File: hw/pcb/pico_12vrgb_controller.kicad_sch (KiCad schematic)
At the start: 20 parts, among them J1 Conn_01x04_RGB, J2 Conn_01x04_RGB, J3 Conn_01x04_RGB, J4 Conn_01x04_RGB, J5 Conn_01x03_Male, J6 Conn_01x03_Male, J7 Conn_01x15_SATA_PWR, Q1 DMG2302U, Q10 DMG2302U, Q11 DMG2302U, Q12 DMG2302U, Q2 DMG2302U, Q3 DMG2302U, Q4 DMG2302U, Q5 DMG2302U, Q6 DMG2302U, Q7 DMG2302U, Q8 DMG2302U, Q9 DMG2302U, U1 Raspberry_Pi_Pico

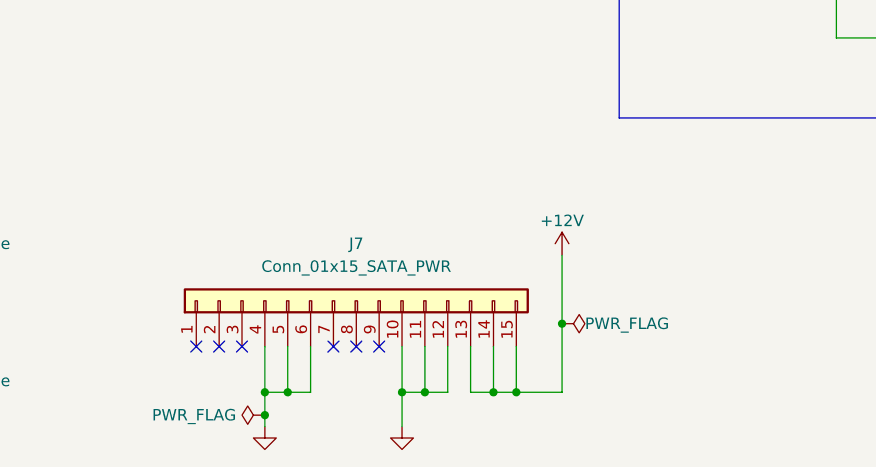
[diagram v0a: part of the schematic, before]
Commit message: Add custom model and footprint for SATA connector
I might need to change this, because the ModDIY listing shows two
different connectors in the pictures, but only has one data sheet
picture. Hopefully both connectors work with the same footprint.
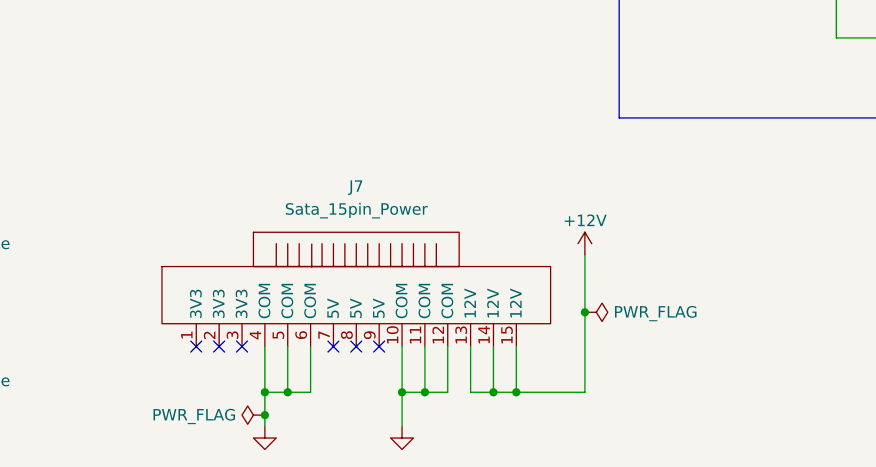
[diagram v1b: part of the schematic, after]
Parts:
- removed J7: Conn_01x15_SATA_PWR, symbol Connector_Generic:Conn_01x15
- added J7: Sata_15pin_Power, pico_12vrgb_controller:ModDIY_SATA_15pin_RightAngle_Header, symbol pico_12vrgb:Sata_15pin_Power
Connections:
- net +12V: now also J7.13 (12V), J7.14 (12V), J7.15 (12V)
- net GND: now also J7.10 (COM), J7.11 (COM), J7.12 (COM), J7.4 (COM), J7.5 (COM), J7.6 (COM)

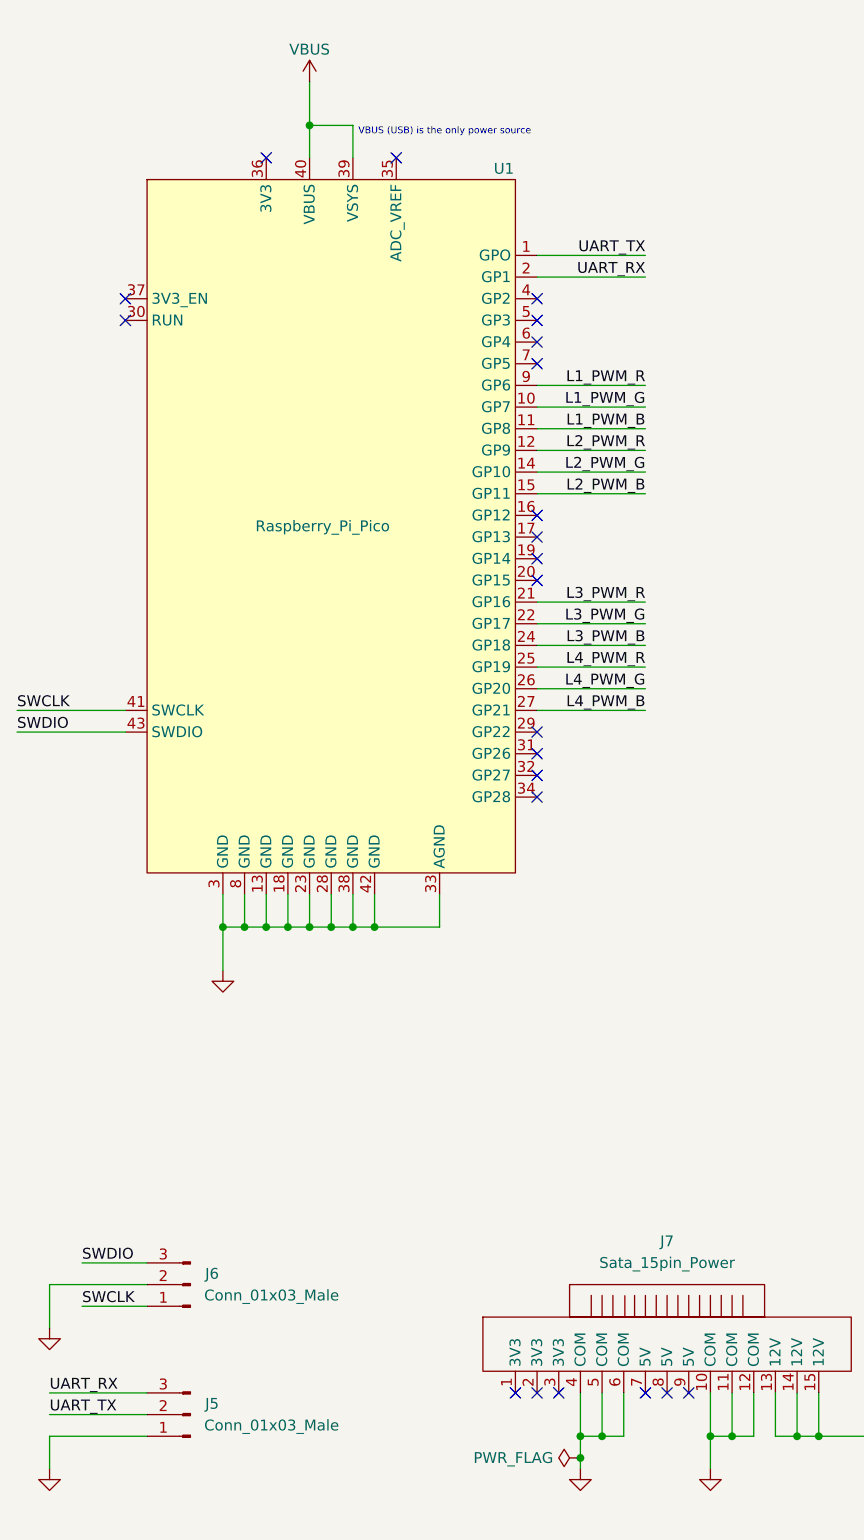
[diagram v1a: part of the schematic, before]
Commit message: Add ADC reference to schematic
Planning to use the internal temperature sensor and given the small
voltages involved, adding a reference sounds like a good idea.

Also changes the UART header to be 4 pins, which seems more conventional
even though the power pin will be disconnected.
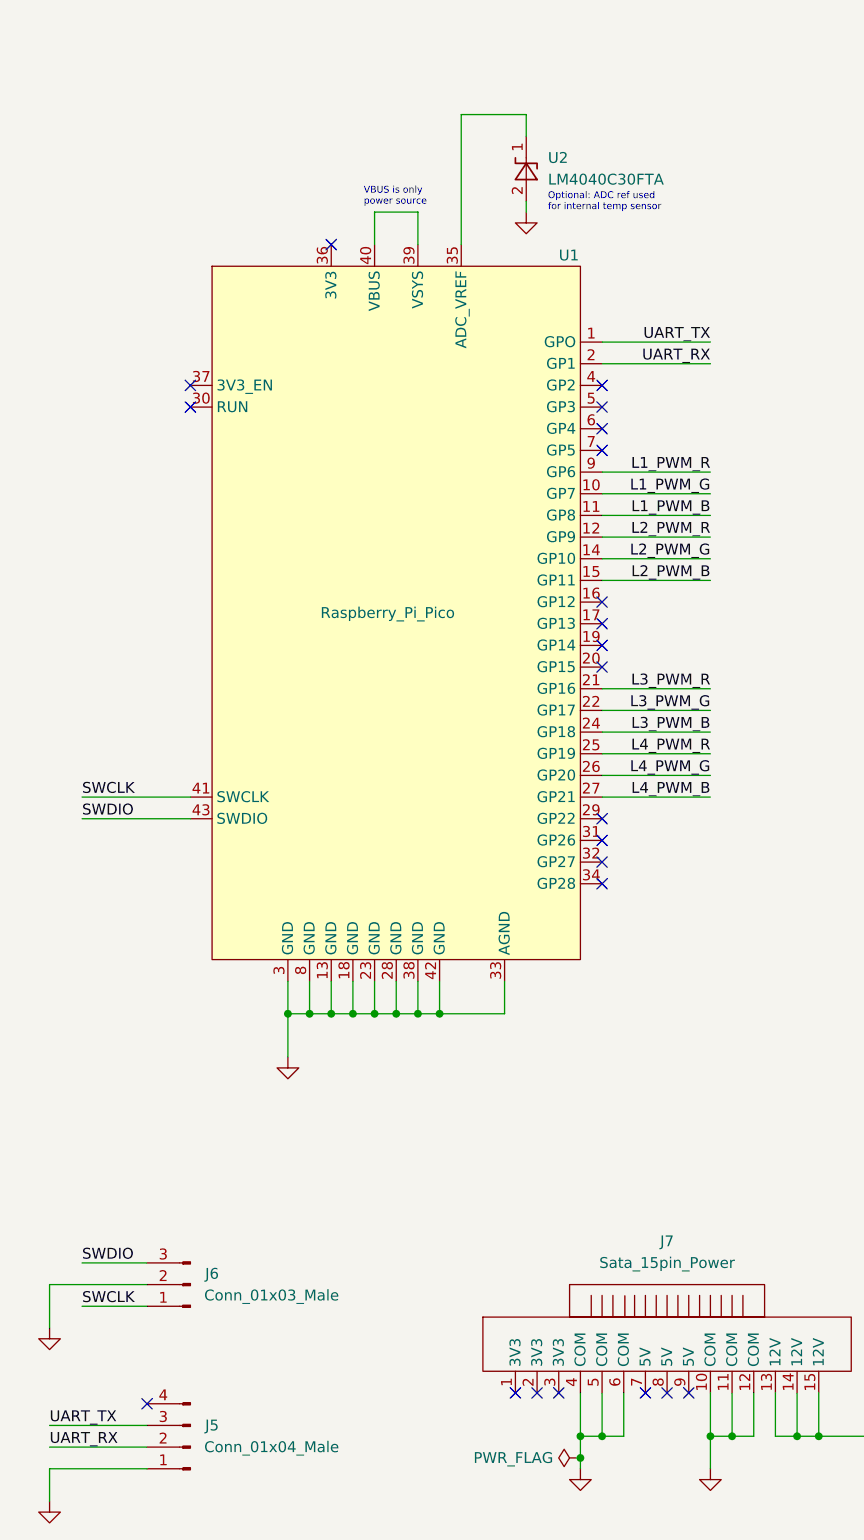
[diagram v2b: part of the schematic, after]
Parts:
- removed J5: Conn_01x03_Male, Connector_PinHeader_2.54mm:PinHeader_1x03_P2.54mm_Vertical, symbol Connector:Conn_01x03_Male
- added J5: Conn_01x04_Male, Connector_PinHeader_2.54mm:PinHeader_1x04_P2.54mm_Vertical, symbol Connector:Conn_01x04_Male
- added U2: LM4040C30FTA, Package_TO_SOT_SMD:SOT-23, symbol Reference_Voltage:LM4040DBZ-3
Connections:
- net GND: now also J5.1 (Pin_1), U2.2 (A)
- net UART_RX: now also J5.2 (Pin_2)
- net UART_TX: now also J5.3 (Pin_3)
- net at U1.35 (ADC_VREF): now also U2.1 (K)
- net VBUS: no longer names the net of U1.39 (VSYS), U1.40 (VBUS)
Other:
- note added: "Optional: ADC ref used for internal temp sensor"
- note added: "VBUS is only power source"
- note removed: "VBUS (USB) is the only power source"
- moved on the sheet: U1

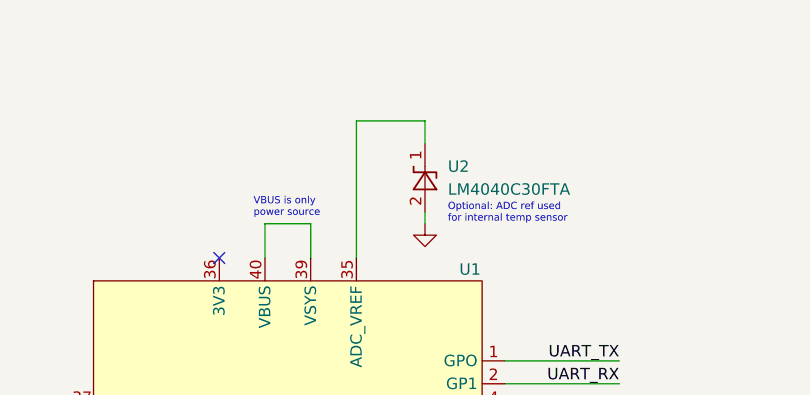
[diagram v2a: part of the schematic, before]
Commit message: Start routing PCB, change header orientation
The RGB half is mostly complete, although I might shift things around to
save a bit of space. Still need to connect things up to the Pico.
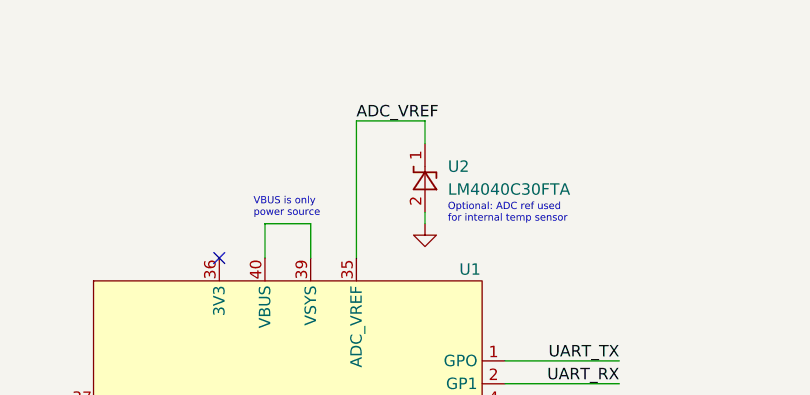
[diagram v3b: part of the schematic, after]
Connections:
- net ADC_VREF: now reaches U1.35 (ADC_VREF), U2.1 (K)
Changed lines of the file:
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@@
+    (effects (font (size 1.27 1.27)) (justify left bottom))
+  )
+  (label "ADC_VREF" (at 73.66 29.21 0)
     (effects (font (size 1.27 1.27)) (justify left bottom))
   )

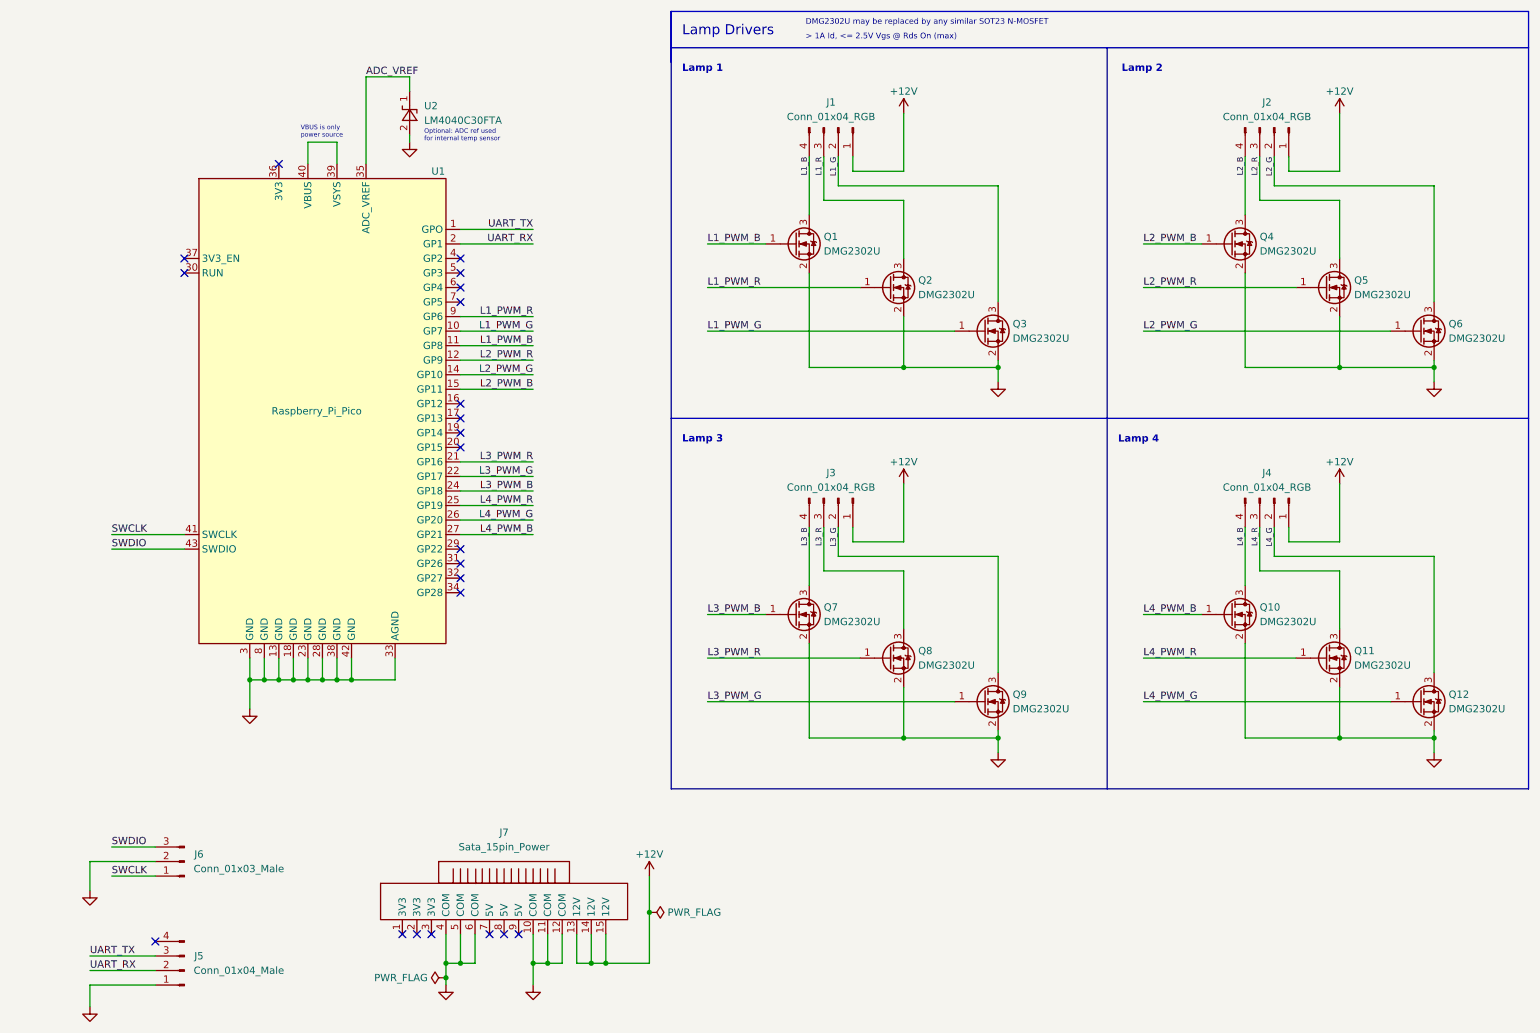
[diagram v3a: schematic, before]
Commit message: Finish PCB routing
Reduce the size of the PCB to 5 square inches, although I could probably
get it a bit smaller. Update the RGB header footprints with the correct
pin sizes and nice labels. Finally, reassign PWM pins to enable cleaner
routing.

There's a bunch of DRC failures because I drew a shape over some traces
instead of using a fill zone. I'll have to try this again and see if I
can get the fill zone to do what I want.
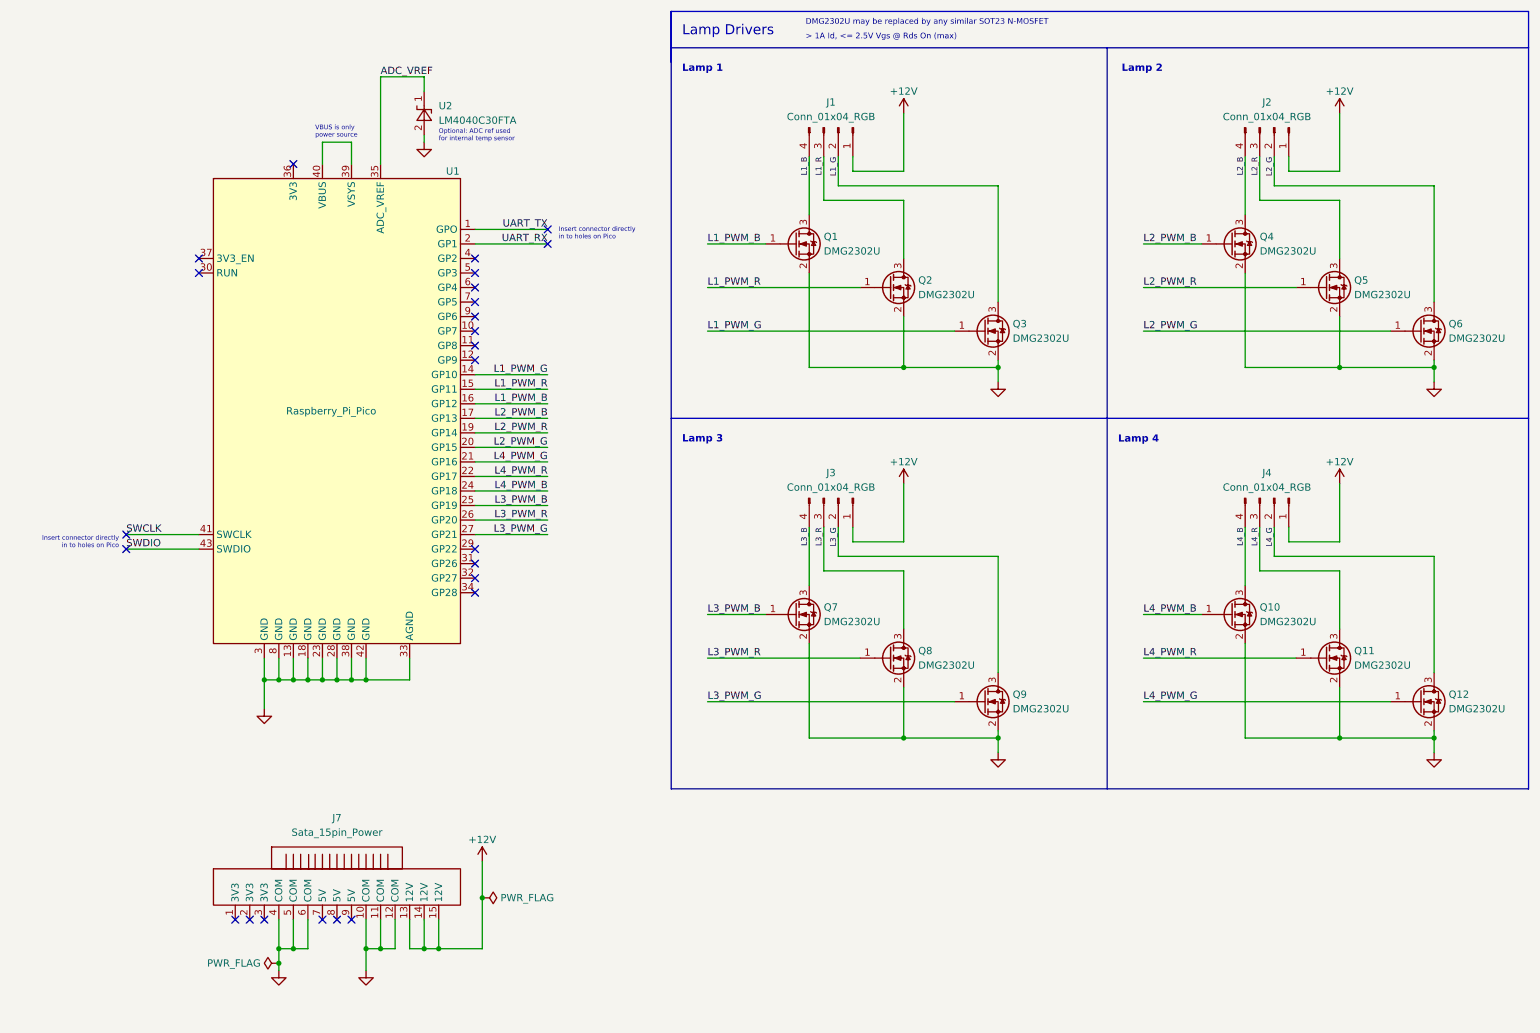
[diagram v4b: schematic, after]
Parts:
- removed J5: Conn_01x04_Male, Connector_PinHeader_2.54mm:PinHeader_1x04_P2.54mm_Vertical, symbol Connector:Conn_01x04_Male
- removed J6: Conn_01x03_Male, Connector_PinHeader_2.54mm:PinHeader_1x03_P2.54mm_Vertical, symbol Connector:Conn_01x03_Male
- J1, J2: footprint Connector_PinHeader_2.54mm:PinHeader_1x04_P2.54mm_Vertical -> pico_12vrgb_controller:PinHeader_12VGRB_Vertical_LeftText
- J3, J4: footprint Connector_PinHeader_2.54mm:PinHeader_1x04_P2.54mm_Vertical -> pico_12vrgb_controller:PinHeader_12VGRB_Vertical_RightText
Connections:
- net L1_PWM_B: now also U1.16 (GP12); no longer U1.11 (GP8)
- net L1_PWM_G: now also U1.14 (GP10); no longer U1.10 (GP7)
- net L1_PWM_R: now also U1.15 (GP11); no longer U1.9 (GP6)
- net L2_PWM_B: now also U1.17 (GP13); no longer U1.15 (GP11)
- net L2_PWM_G: now also U1.20 (GP15); no longer U1.14 (GP10)
- net L2_PWM_R: now also U1.19 (GP14); no longer U1.12 (GP9)
- net L3_PWM_B: now also U1.25 (GP19); no longer U1.24 (GP18)
- net L3_PWM_G: now also U1.27 (GP21); no longer U1.22 (GP17)
- net L3_PWM_R: now also U1.26 (GP20); no longer U1.21 (GP16)
- net L4_PWM_B: now also U1.24 (GP18); no longer U1.27 (GP21)
- net L4_PWM_G: now also U1.21 (GP16); no longer U1.26 (GP20)
- net L4_PWM_R: now also U1.22 (GP17); no longer U1.25 (GP19)
- no-connect marks 22 -> 25
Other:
- note added: "Insert connector directly in to holes on Pico"
- moved on the sheet: J7, U1, U2

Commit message: Fix 12V fill, minor PCB layout tweaks
Clean up silkscreen, fix remaining DRC errors, expand pads on RGB header
footprints, make the board slightly shorter on the USB end.
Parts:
- renumbered J7 to J5
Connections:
- net VBUS: now reaches U1.39 (VSYS), U1.40 (VBUS)
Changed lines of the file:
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@@
     (effects (font (size 1.27 1.27) (thickness 0.254) bold) (justify left bottom))
   )
-  (text "VBUS is only\npower source" (at 64.77 40.005 0)
+  (text "VBUS is only\npower source" (at 64.77 38.1 0)
     (effects (font (size 0.8 0.8)) (justify left bottom))
   )
@@
     (effects (font (size 1.27 1.27)) (justify left bottom))
   )
+  (label "VBUS" (at 66.04 40.64 0)
+    (effects (font (size 1.27 1.27)) (justify left bottom))
+  )
   (label "L3_PWM_G" (at 133.35 138.43 0)
     (effects (font (size 1.27 1.27)) (justify left bottom))
@@
   (symbol (lib_id "pico_12vrgb:Sata_15pin_Power") (at 68.58 173.99 0) (unit 1)
     (in_bom yes) (on_board yes) (fields_autoplaced)
-    (property "Reference" "J7" (id 0) (at 68.58 158.75 0))
+    (property "Reference" "J5" (id 0) (at 68.58 158.75 0))
     (property "Value" "Sata_15pin_Power" (id 1) (at 68.58 161.29 0))
     (property "Footprint" "pico_12vrgb_controller:ModDIY_SATA_15pin_RightAngle_Header" (id 2) (at 67.31 189.23 0)
@@
     )
     (path "/0f977c57-1c1d-490f-9438-a3a505308806"
-      (reference "J7") (unit 1) (value "Sata_15pin_Power") (footprint "pico_12vrgb_controller:ModDIY_SATA_15pin_RightAngle_Header")
+      (reference "J5") (unit 1) (value "Sata_15pin_Power") (footprint "pico_12vrgb_controller:ModDIY_SATA_15pin_RightAngle_Header")
     )
     (path "/3256f776-773f-456f-9fda-6c6db2f88e00"
